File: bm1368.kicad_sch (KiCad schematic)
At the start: 59 parts, among them U1 25MHz, U4 BM1368_mode1, U5 MCP1824T-1202E/OT, U6 MCP1824T-0802E, U8 SN74AVC4T774

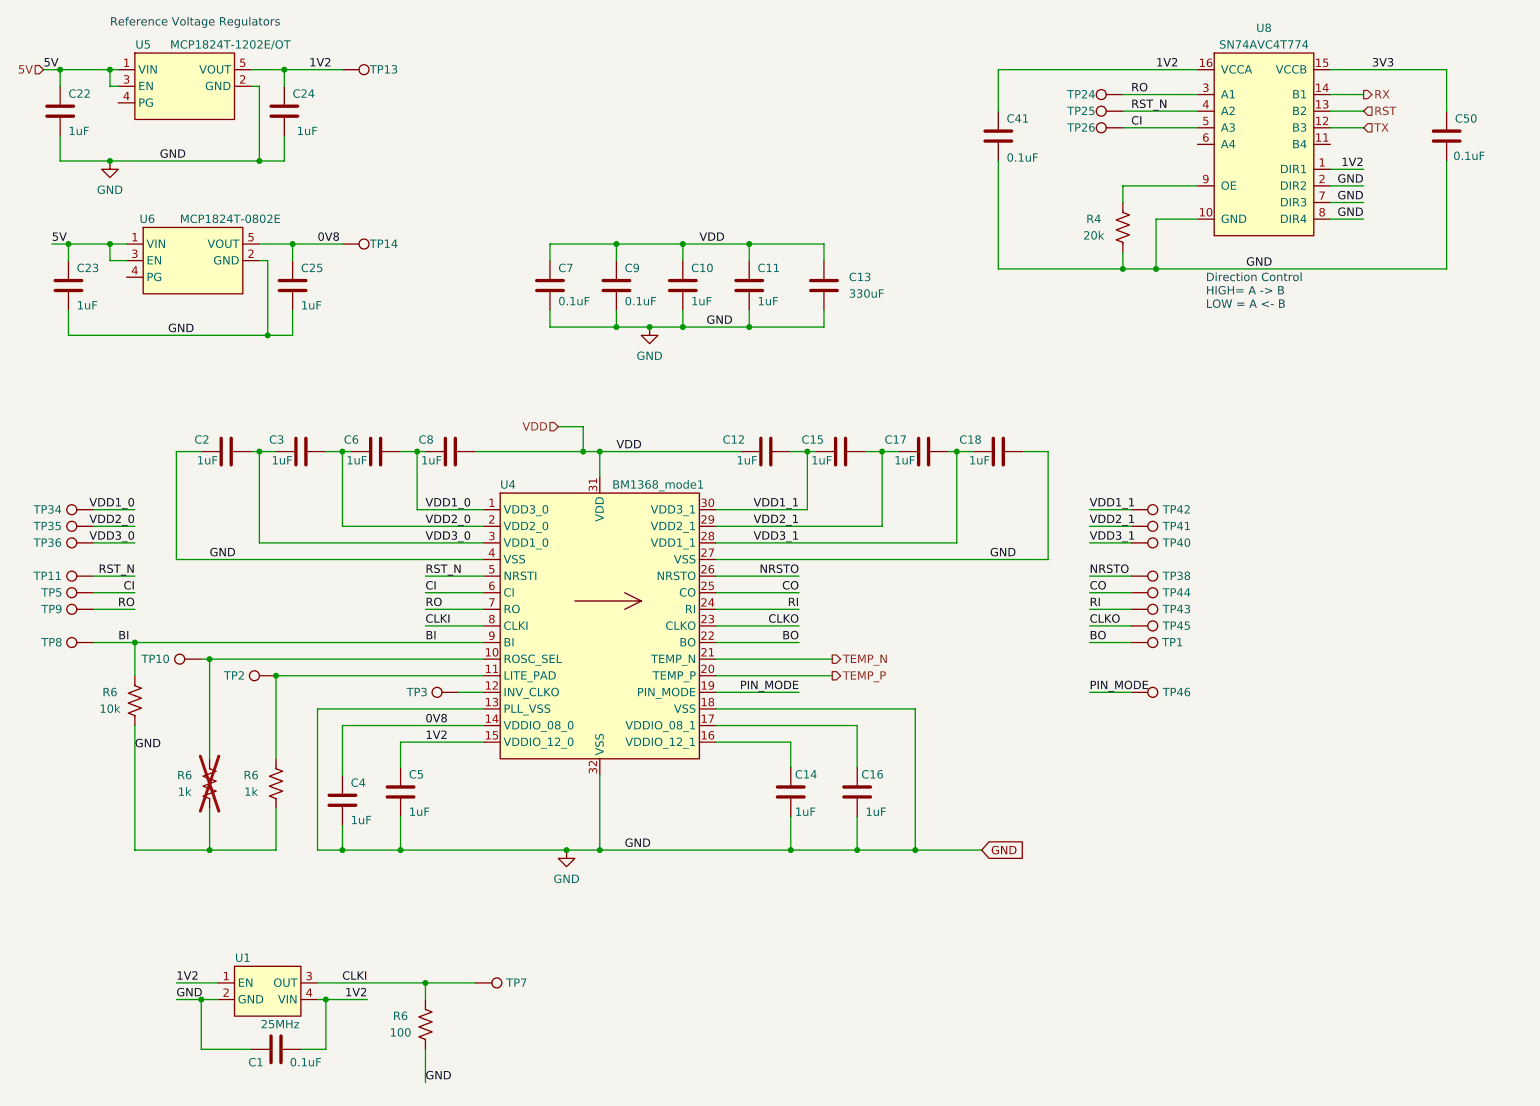
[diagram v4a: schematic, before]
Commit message: mostly routed. still need some power routing
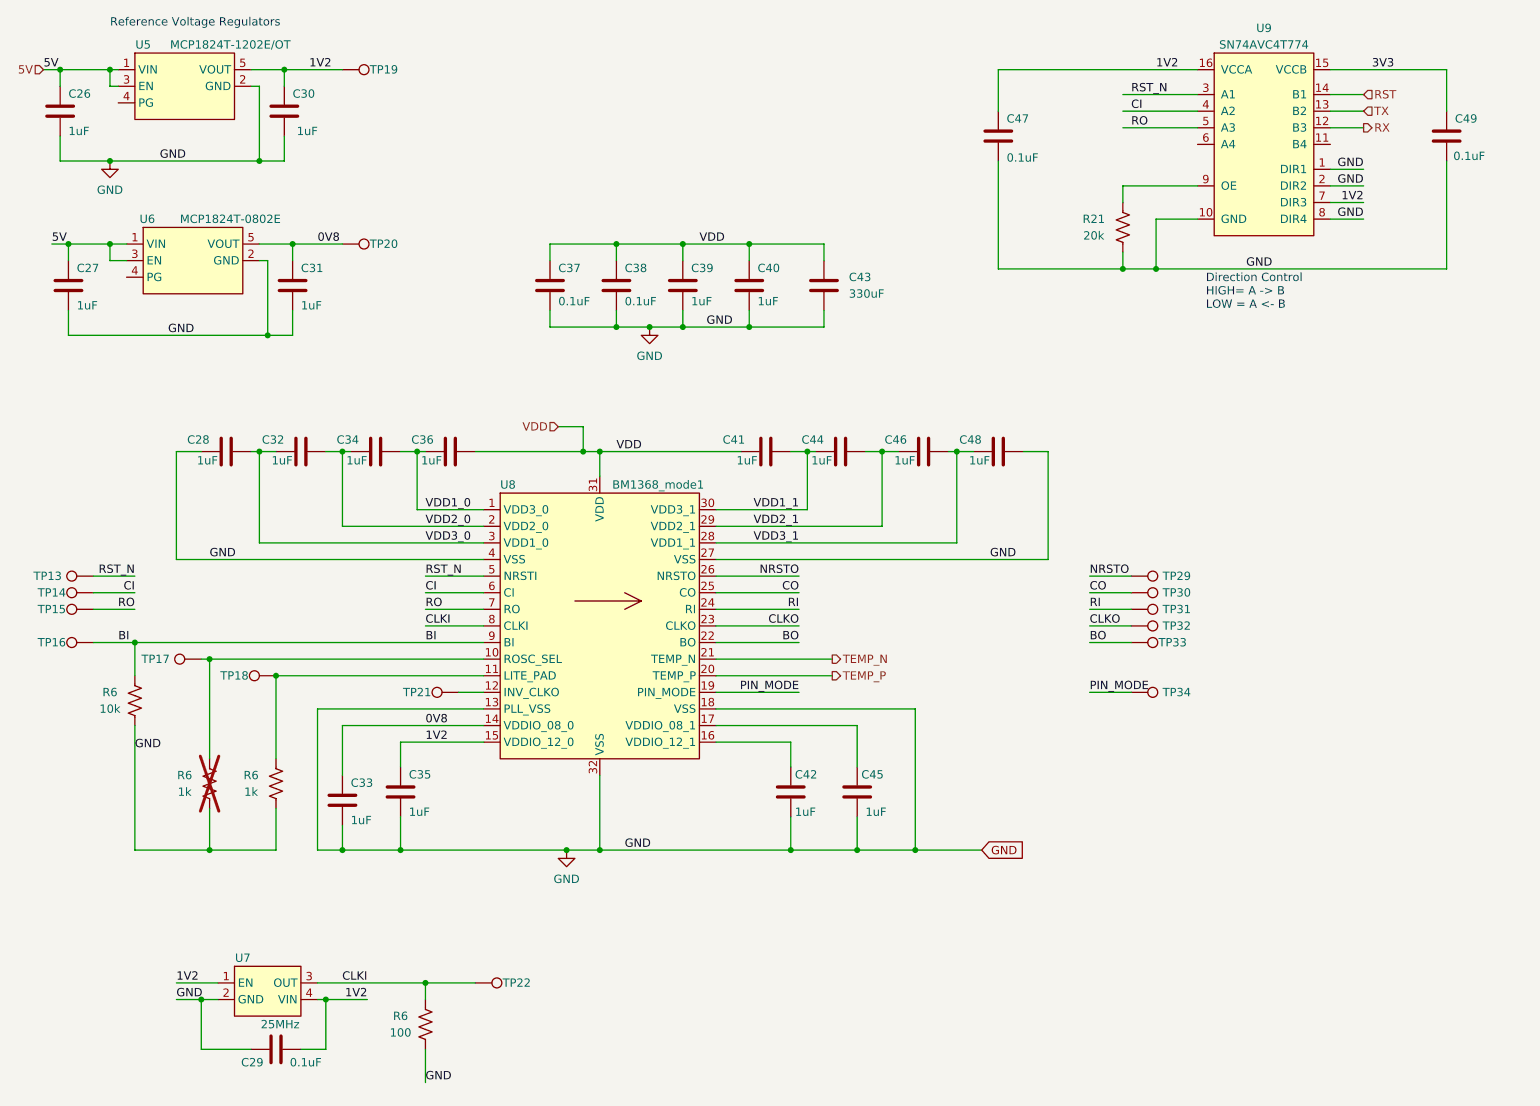
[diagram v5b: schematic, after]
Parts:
- removed TP24, TP25, TP26, TP34, TP35, TP36, TP40, TP41, TP42: TestPoint, TestPoint:TestPoint_Pad_D1.5mm, symbol Connector:TestPoint
- renumbered C22 to C26, C23 to C27, C2 to C28, C1 to C29, C24 to C30, C25 to C31, C3 to C32, C4 to C33, C6 to C34, C5 to C35, C8 to C36, C7 to C37, C9 to C38, C10 to C39, C11 to C40, C12 to C41, C14 to C42, C13 to C43, C15 to C44, C16 to C45, C17 to C46, C41 to C47, C18 to C48, C50 to C49, R4 to R21, TP11 to TP13, TP5 to TP14, TP9 to TP15, TP8 to TP16, TP10 to TP17, TP2 to TP18, TP13 to TP19, TP14 to TP20, TP3 to TP21, TP7 to TP22, TP38 to TP29, TP44 to TP30, TP43 to TP31, TP45 to TP32, TP1 to TP33, TP46 to TP34, U1 to U7, U4 to U8, U8 to U9
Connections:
- net 1V2: now also U9.7 (DIR3); no longer U9.1 (DIR1)
- net CI: now also U9.4 (A2); no longer U9.5 (A3)
- net GND: now also U9.1 (DIR1); no longer U9.7 (DIR3)
- net RO: now also U9.5 (A3); no longer U9.3 (A1)
- net RST: now also U9.14 (B1); no longer U9.13 (B2)
- net RST_N: now also U9.3 (A1); no longer U9.4 (A2)
- net RX: now also U9.12 (B3); no longer U9.14 (B1)
- net TX: now also U9.13 (B2); no longer U9.12 (B3)

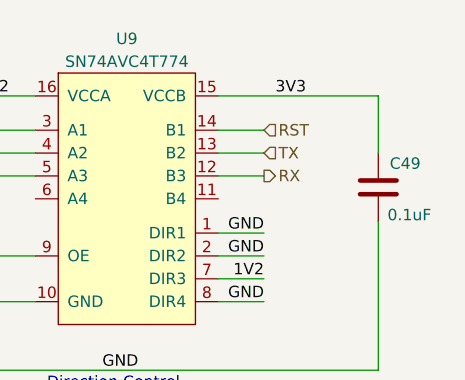
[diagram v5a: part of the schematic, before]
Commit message: placed all the silkscreen, finished routing, DRC is looking pretty good
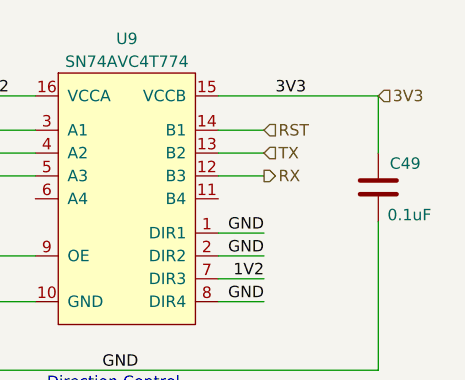
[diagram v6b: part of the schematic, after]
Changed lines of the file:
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@@
+		)
+	)
+	(hierarchical_label "3V3"
+		(shape input)
+		(at 242.57 29.21 0)
+		(fields_autoplaced yes)
+		(effects
+			(font
+				(size 1.27 1.27)
+			)
+			(justify left)
 		)
 	)

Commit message: some changes for ERC
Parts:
- R6: now not fitted; now left out of the parts list
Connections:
- net GND: now also U9.6 (A4)
- no-connect marks 0 -> 3
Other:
- moved on the sheet: C33, R6

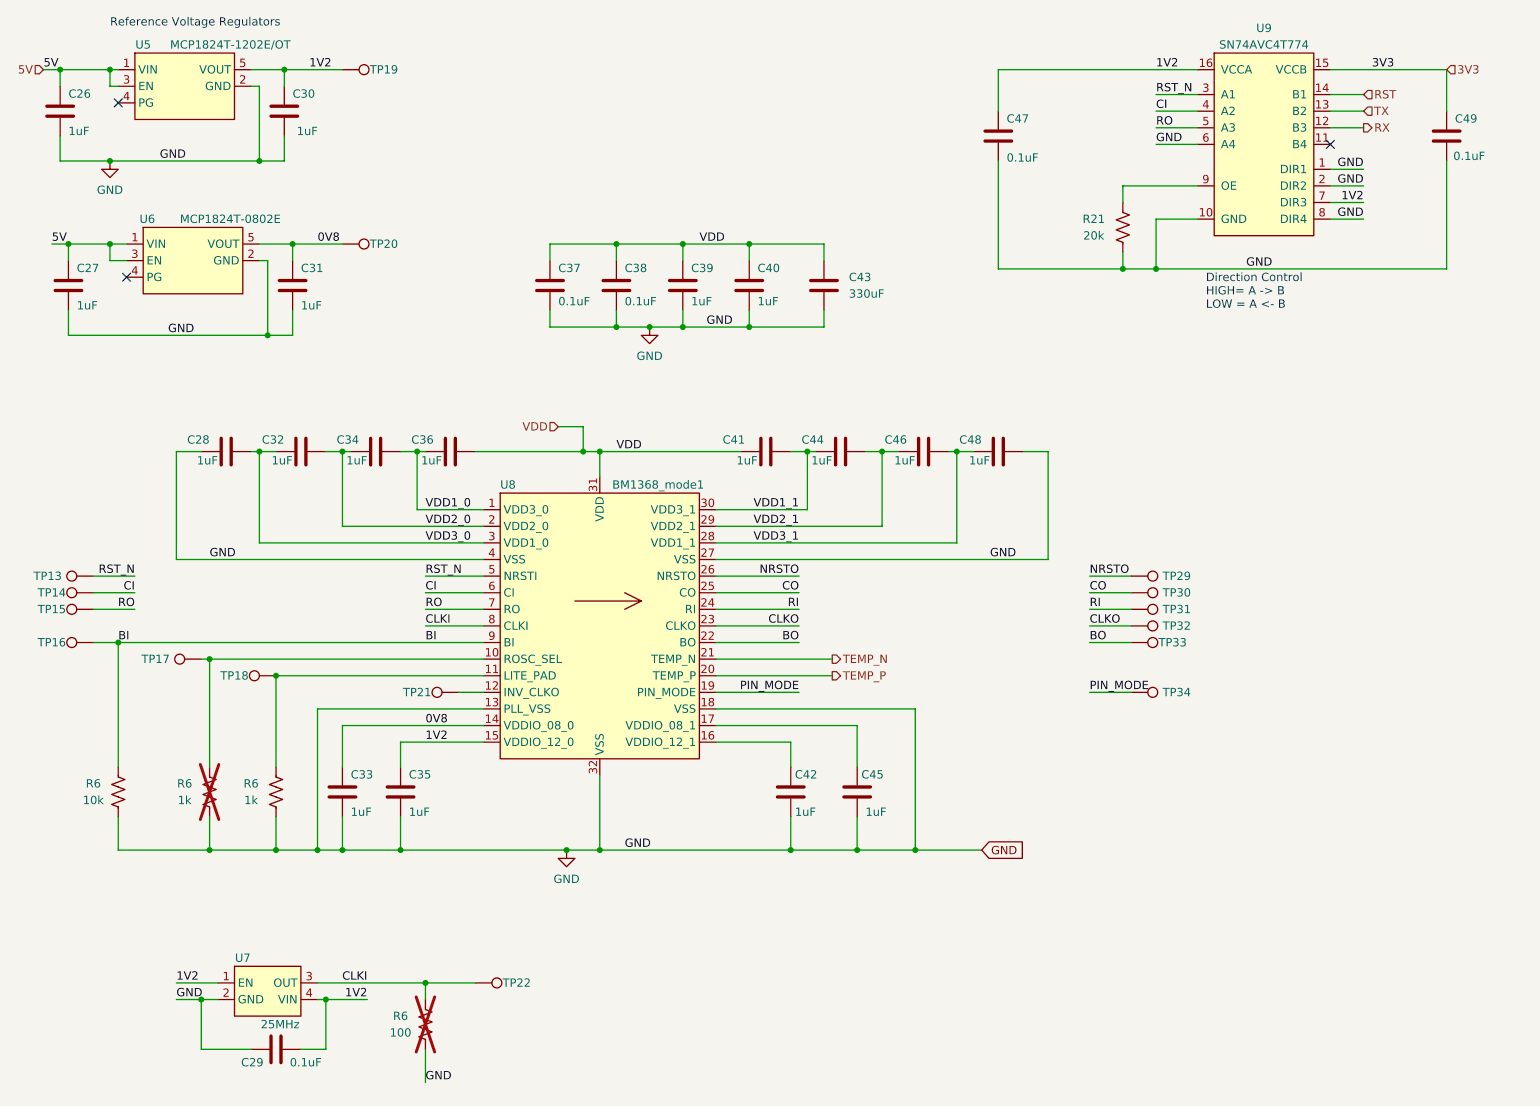
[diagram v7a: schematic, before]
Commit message: added DK partnumbers and exported BOM
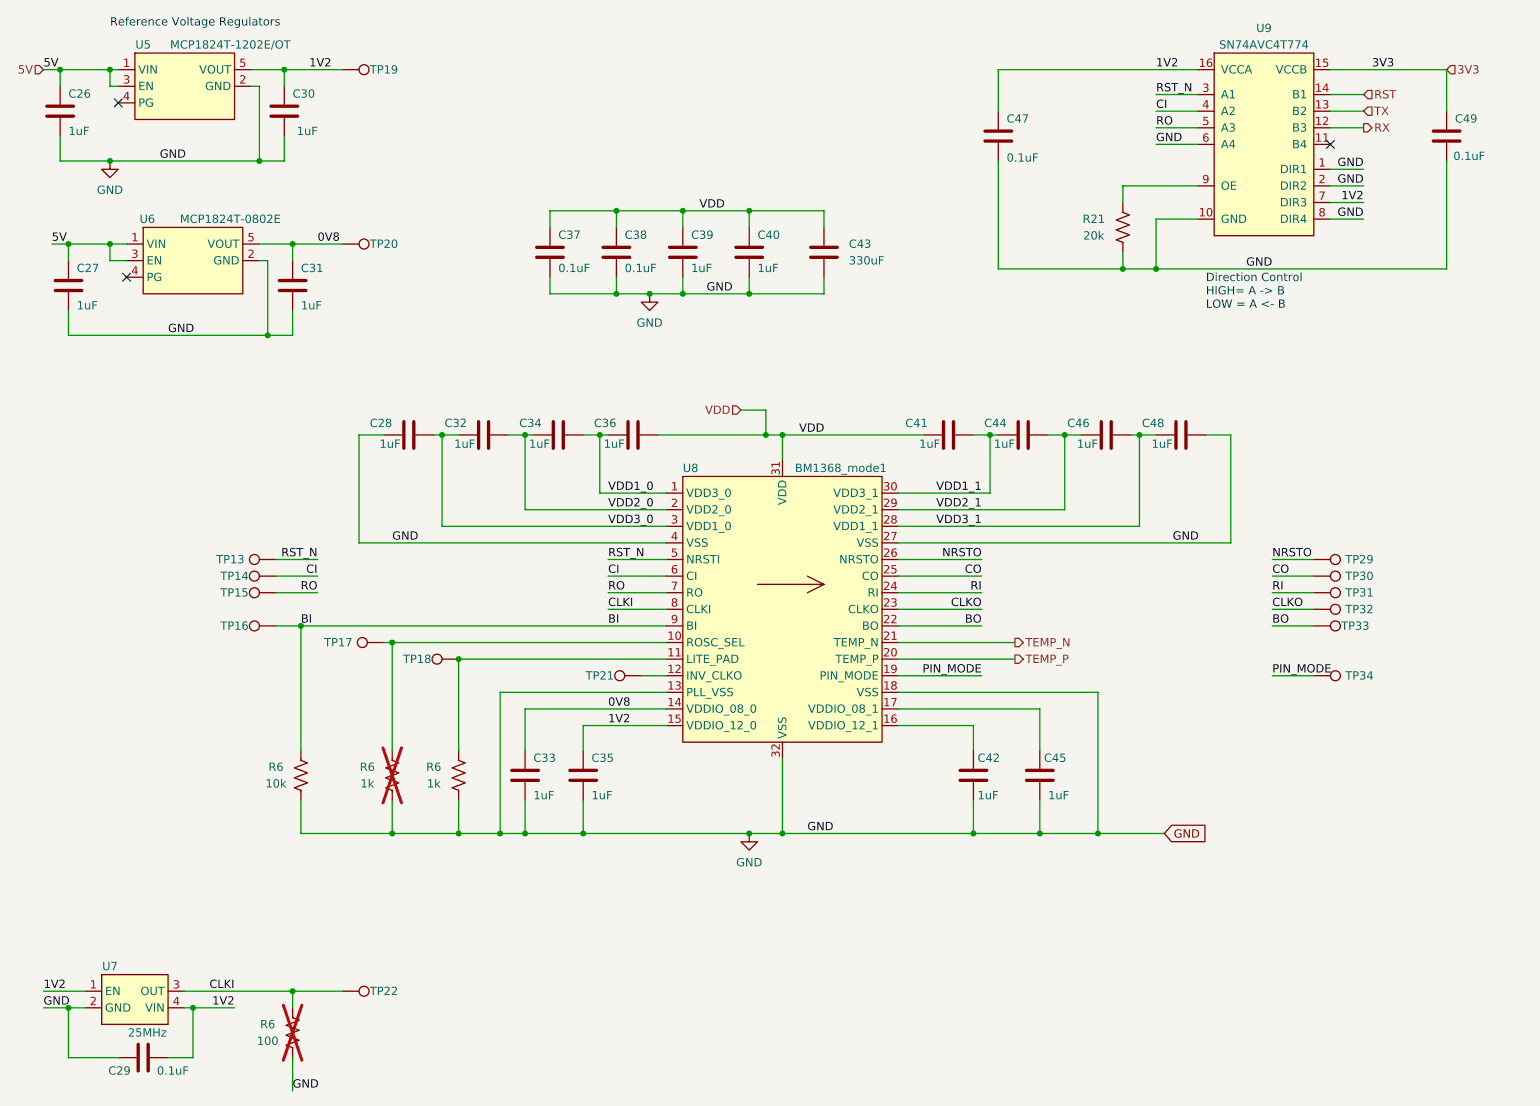
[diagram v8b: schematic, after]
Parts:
- C37, C38: DK 478-KGM05AR71C104KHTR-ND -> 1292-1639-1-ND; PARTNO KGM05AR71C104KH -> 0402X104K100CT
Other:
- moved on the sheet: C28, C29, C32, C33, C34, C35, C36, C37, C38, C39, C40, C41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
